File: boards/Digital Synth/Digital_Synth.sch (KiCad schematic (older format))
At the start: 32 parts, among them J5 Barrel_Jack, J6 JTAG, J7 Micro_SD_Card, SW1 SW_Push, SW2 SW_Push, U1 LM1117-3.3, U5 STM32F405RGTx, Y1 12MHz

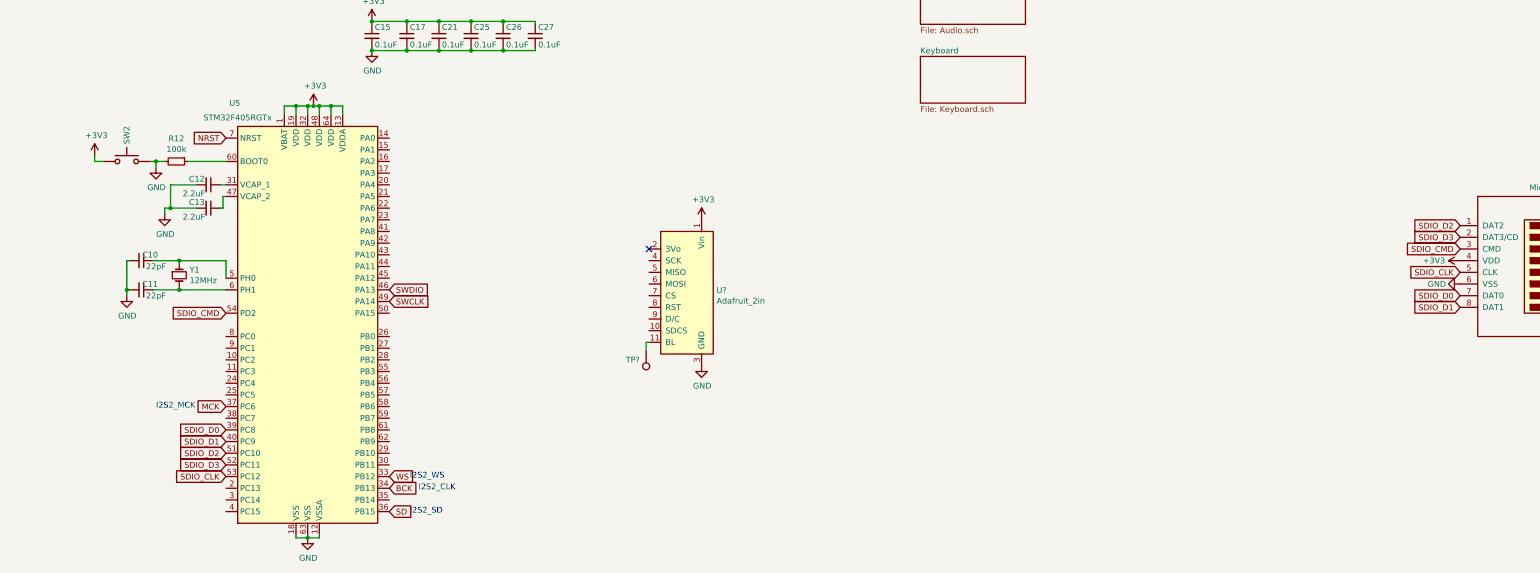
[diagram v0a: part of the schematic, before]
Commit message: added display
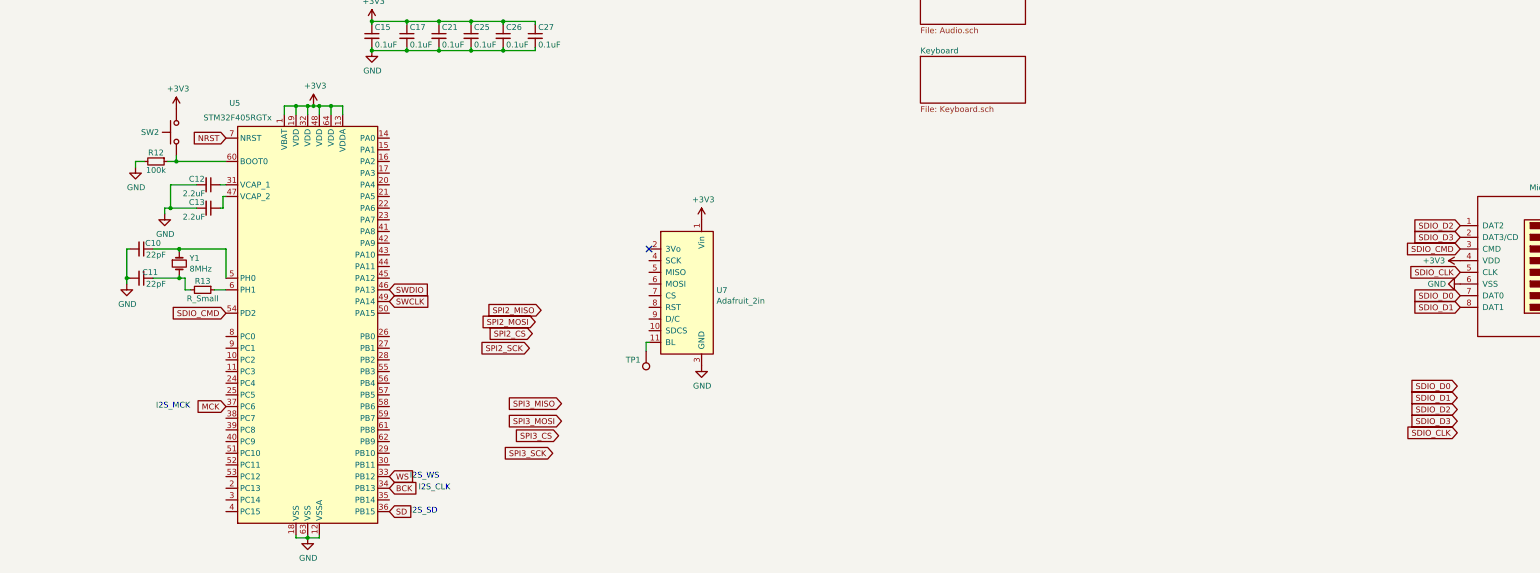
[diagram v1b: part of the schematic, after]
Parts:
- added R13: R_Small, symbol device:R_Small
- C10, C11, C12, C13: footprint (none) -> Capacitor_SMD:C_0603_1608Metric_Pad1.05x0.95mm_HandSolder
- SW1, SW2: footprint (none) -> Button_Switch_THT:SW_PUSH_6mm
- U7: renamed from U?; footprint (none) -> Display:Adafruit_2in
- Y1: value 12MHz -> 8MHz; footprint (none) -> Crystal:Crystal_HC49-U_Vertical
- gave numbers to parts that had none: 1
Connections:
- net +3V3: now also SW2.2; no longer SW2.1
- net GND: no longer SW2.2
- net SDIO_CLK: no longer U5.53 (PC12)
- net SDIO_D0: no longer U5.39 (PC8)
- net SDIO_D1: no longer U5.40 (PC9)
- net SDIO_D2: no longer U5.51 (PC10)
- net SDIO_D3: no longer U5.52 (PC11)
- net at C11.1, Y1.2: now also R13.2; no longer U5.6 (PH1)
- net at R12.1, U5.60 (BOOT0): now also SW2.1
- new net: R13.1, U5.6 (PH1)
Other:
- note added: "I2S_CLK"
- note added: "I2S_MCK"
- note added: "I2S_SD"
- note added: "I2S_WS"
- note removed: "I2S2_CLK"
- note removed: "I2S2_MCK"
- note removed: "I2S2_SD"
- note removed: "I2S2_WS"
- moved on the sheet: C10, C11, R12, SW2, Y1
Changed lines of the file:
@@
-$EndComp
-$Comp
-L MCU_ST_STM32F4:STM32F405RGTx U5
-U 1 1 622C0233
-P 6025 4000
-F 0 "U5" H 5400 5900 50  0000 C CNN
-F 1 "STM32F405RGTx" H 5425 5775 50  0000 C CNN
-F 2 "Package_QFP:LQFP-64_10x10mm_P0.5mm" H 5425 2300 50  0001 R CNN
-F 3 "http://www.st.com/st-web-ui/static/active/en/resource/technical/document/datasheet/DM00037051.pdf" H 6025 4000 50  0001 C CNN
-	1    6025 4000
-	1    0    0    -1
 $EndComp
 $Comp
@@
 L power:GND #PWR016
 U 1 1 622DC5D8
-P 4725 2650
-F 0 "#PWR016" H 4725 2400 50  0001 C CNN
-F 1 "GND" H 4730 2477 50  0000 C CNN
-F 2 "" H 4725 2650 50  0001 C CNN
-F 3 "" H 4725 2650 50  0001 C CNN
-	1    4725 2650
-	1    0    0    -1
-$EndComp
-$Comp
-L device:R_Small R12
-U 1 1 622DDA0B
-P 4900 2600
-F 0 "R12" V 4704 2600 50  0000 C CNN
-F 1 "100k" V 4795 2600 50  0000 C CNN
-F 2 "Resistor_SMD:R_0805_2012Metric_Pad1.15x1.40mm_HandSolder" H 4900 2600 50  0001 C CNN
-F 3 "~" H 4900 2600 50  0001 C CNN
-	1    4900 2600
-	0    1    1    0
-$EndComp
-Wire Wire Line
-	5000 2600 5325 2600
-Wire Wire Line
-	4800 2600 4725 2600
-Wire Wire Line
-	4725 2600 4725 2650
+P 4550 2650
+F 0 "#PWR016" H 4550 2400 50  0001 C CNN
+F 1 "GND" H 4555 2477 50  0000 C CNN
+F 2 "" H 4550 2650 50  0001 C CNN
+F 3 "" H 4550 2650 50  0001 C CNN
+	1    4550 2650
+	1    0    0    -1
+$EndComp
 Text Notes 6900 5625 0    50   ~ 0
-I2S2_SD
+I2S_SD
 Text Notes 6975 5425 0    50   ~ 0
-I2S2_CLK
+I2S_CLK
 Text Notes 6900 5325 0    50   ~ 0
-I2S2_WS
+I2S_WS
 Text Notes 4725 4725 0    50   ~ 0
-I2S2_MCK
+I2S_MCK
 Text GLabel 5325 4700 0    50   Input ~ 0
 MCK
@@
 L device:Crystal_Small Y1
 U 1 1 6252B917
-P 4925 3575
-F 0 "Y1" V 4879 3663 50  0000 L CNN
-F 1 "12MHz" V 4970 3663 50  0000 L CNN
-F 2 "" H 4925 3575 50  0001 C CNN
-F 3 "~" H 4925 3575 50  0001 C CNN
-	1    4925 3575
+P 4925 3475
+F 0 "Y1" V 4879 3563 50  0000 L CNN
+F 1 "8MHz" V 4970 3563 50  0000 L CNN
+F 2 "Crystal:Crystal_HC49-U_Vertical" H 4925 3475 50  0001 C CNN
+F 3 "~" H 4925 3475 50  0001 C CNN
+	1    4925 3475
 	0    1    1    0
 $EndComp
-Wire Wire Line
-	5325 3450 5325 3600
 $Comp
 L device:C_Small C10
 U 1 1 62533AA6
-P 4600 3450
-F 0 "C10" V 4550 3525 50  0000 C CNN
-F 1 "22pF" V 4650 3575 50  0000 C CNN
-F 2 "" H 4600 3450 50  0001 C CNN
-F 3 "~" H 4600 3450 50  0001 C CNN
-	1    4600 3450
+P 4600 3350
+F 0 "C10" V 4550 3450 50  0000 C CNN
+F 1 "22pF" V 4650 3475 50  0000 C CNN
+F 2 "Capacitor_SMD:C_0603_1608Metric_Pad1.05x0.95mm_HandSolder" H 4600 3350 50  0001 C CNN
+F 3 "~" H 4600 3350 50  0001 C CNN
+	1    4600 3350
 	0    1    1    0
 $EndComp
@@
 L device:C_Small C11
 U 1 1 6253A48D
-P 4600 3700
-F 0 "C11" V 4550 3775 50  0000 C CNN
-F 1 "22pF" V 4650 3825 50  0000 C CNN
-F 2 "" H 4600 3700 50  0001 C CNN
-F 3 "~" H 4600 3700 50  0001 C CNN
-	1    4600 3700
+P 4600 3600
+F 0 "C11" V 4550 3675 50  0000 C CNN
+F 1 "22pF" V 4650 3725 50  0000 C CNN
+F 2 "Capacitor_SMD:C_0603_1608Metric_Pad1.05x0.95mm_HandSolder" H 4600 3600 50  0001 C CNN
+F 3 "~" H 4600 3600 50  0001 C CNN
+	1    4600 3600
 	0    1    1    0
 $EndComp
@@
 L power:GND #PWR015
 U 1 1 62542EEB
-P 4475 3750
-F 0 "#PWR015" H 4475 3500 50  0001 C CNN
-F 1 "GND" H 4480 3577 50  0000 C CNN
-F 2 "" H 4475 3750 50  0001 C CNN
-F 3 "" H 4475 3750 50  0001 C CNN
-	1    4475 3750
-	1    0    0    -1
-$EndComp
-Wire Wire Line
-	4500 3700 4475 3700
-Wire Wire Line
-	4475 3700 4475 3750
-Wire Wire Line
-	4500 3450 4475 3450
-Wire Wire Line
-	4475 3450 4475 3700
-Connection ~ 4475 3700
+P 4475 3650
+F 0 "#PWR015" H 4475 3400 50  0001 C CNN
+F 1 "GND" H 4480 3477 50  0000 C CNN
+F 2 "" H 4475 3650 50  0001 C CNN
+F 3 "" H 4475 3650 50  0001 C CNN
+	1    4475 3650
+	1    0    0    -1
+$EndComp
+Wire Wire Line
+	4500 3600 4475 3600
+Wire Wire Line
+	4475 3600 4475 3650
+Wire Wire Line
+	4500 3350 4475 3350
+Wire Wire Line
+	4475 3350 4475 3600
+Connection ~ 4475 3600
 $Comp
 L device:LED_Small D33
@@
 F 0 "SW1" V 1425 4123 50  0000 L CNN
 F 1 "SW_Push" V 1470 4123 50  0001 L CNN
-F 2 "" H 1425 4175 50  0001 C CNN
+F 2 "Button_Switch_THT:SW_PUSH_6mm" H 1425 4175 50  0001 C CNN
 F 3 "" H 1425 4175 50  0001 C CNN
 	1    1425 3975
@@
 L Switch:SW_Push SW2
 U 1 1 62582EF8
-P 4475 2600
-F 0 "SW2" V 4475 2748 50  0000 L CNN
-F 1 "SW_Push" V 4520 2748 50  0001 L CNN
-F 2 "" H 4475 2800 50  0001 C CNN
-F 3 "" H 4475 2800 50  0001 C CNN
-	1    4475 2600
-	1    0    0    -1
-$EndComp
-Wire Wire Line
-	4675 2600 4725 2600
-Connection ~ 4725 2600
+P 4900 2350
+F 0 "SW2" V 4900 2498 50  0000 L CNN
+F 1 "SW_Push" V 4945 2498 50  0001 L CNN
+F 2 "Button_Switch_THT:SW_PUSH_6mm" H 4900 2550 50  0001 C CNN
+F 3 "" H 4900 2550 50  0001 C CNN
+	1    4900 2350
+	0    -1   -1   0
+$EndComp
 $Comp
 L power:+3V3 #PWR014
 U 1 1 6258A598
-P 4200 2550
-F 0 "#PWR014" H 4200 2400 50  0001 C CNN
-F 1 "+3V3" H 4215 2723 50  0000 C CNN
-F 2 "" H 4200 2550 50  0001 C CNN
-F 3 "" H 4200 2550 50  0001 C CNN
-	1    4200 2550
-	1    0    0    -1
-$EndComp
-Wire Wire Line
-	4200 2550 4200 2600
-Wire Wire Line
-	4200 2600 4275 2600
+P 4900 2150
+F 0 "#PWR014" H 4900 2000 50  0001 C CNN
+F 1 "+3V3" H 4915 2323 50  0000 C CNN
+F 2 "" H 4900 2150 50  0001 C CNN
+F 3 "" H 4900 2150 50  0001 C CNN
+	1    4900 2150
+	1    0    0    -1
+$EndComp
 $Comp
 L device:C_Small C12
@@
 F 0 "C12" V 5125 2700 50  0000 C CNN
 F 1 "2.2uF" V 5250 2675 50  0000 C CNN
-F 2 "" H 5175 2800 50  0001 C CNN
+F 2 "Capacitor_SMD:C_0603_1608Metric_Pad1.05x0.95mm_HandSolder" H 5175 2800 50  0001 C CNN
 F 3 "~" H 5175 2800 50  0001 C CNN
 	1    5175 2800
@@
 F 0 "C13" V 5125 2900 50  0000 C CNN
 F 1 "2.2uF" V 5250 2875 50  0000 C CNN
-F 2 "" H 5175 3000 50  0001 C CNN
+F 2 "Capacitor_SMD:C_0603_1608Metric_Pad1.05x0.95mm_HandSolder" H 5175 3000 50  0001 C CNN
 F 3 "~" H 5175 3000 50  0001 C CNN
 	1    5175 3000
@@
 Connection ~ 1550 5550
 Wire Wire Line
-	4700 3700 4925 3700
-Wire Wire Line
-	4700 3450 4925 3450
-Wire Wire Line
-	4925 3475 4925 3450
-Connection ~ 4925 3450
-Wire Wire Line
-	4925 3450 5325 3450
-Wire Wire Line
-	4925 3675 4925 3700
-Connection ~ 4925 3700
-Wire Wire Line
-	4925 3700 5325 3700
+	4700 3600 4925 3600
+Wire Wire Line
+	4700 3350 4925 3350
+Wire Wire Line
+	4925 3375 4925 3350
+Connection ~ 4925 3350
+Wire Wire Line
+	4925 3350 5325 3350
+Wire Wire Line
+	4925 3575 4925 3600
 $Comp
 L Connector:Micro_SD_Card J7
@@
 Text GLabel 15900 3550 0    50   Input ~ 0
 SDIO_CLK
-Text GLabel 5325 4900 0    50   Input ~ 0
+Text GLabel 15875 4525 0    50   Input ~ 0
 SDIO_D0
-Text GLabel 5325 5000 0    50   Input ~ 0
+Text GLabel 15875 4625 0    50   Input ~ 0
 SDIO_D1
-Text GLabel 5325 5100 0    50   Input ~ 0
+Text GLabel 15875 4725 0    50   Input ~ 0
 SDIO_D2
-Text GLabel 5325 5200 0    50   Input ~ 0
+Text GLabel 15875 4825 0    50   Input ~ 0
 SDIO_D3
 Text GLabel 5325 3900 0    50   Input ~ 0
 SDIO_CMD
-Text GLabel 5325 5300 0    50   Input ~ 0
+Text GLabel 15875 4925 0    50   Input ~ 0
 SDIO_CLK
 $Comp
@@
 NoConn ~ 8950 3350
 $Comp
-L power:GND #PWR?
+L power:GND #PWR0110
 U 1 1 623F4583
 P 9400 4350
-F 0 "#PWR?" H 9400 4100 50  0001 C CNN
+F 0 "#PWR0110" H 9400 4100 50  0001 C CNN
 F 1 "GND" H 9405 4177 50  0000 C CNN
 F 2 "" H 9400 4350 50  0001 C CNN
@@
 $EndComp
 $Comp
-L power:+3V3 #PWR?
+L power:+3V3 #PWR0111
 U 1 1 623ECA3D
 P 9400 3100
-F 0 "#PWR?" H 9400 2950 50  0001 C CNN
+F 0 "#PWR0111" H 9400 2950 50  0001 C CNN
 F 1 "+3V3" H 9415 3273 50  0000 C CNN
 F 2 "" H 9400 3100 50  0001 C CNN
@@
 $EndComp
 $Comp
-L Connector:TestPoint TP?
+L Connector:TestPoint TP1
 U 1 1 6240D6CD
 P 8925 4225
-F 0 "TP?" H 9100 4300 50  0000 R CNN
+F 0 "TP1" H 9100 4300 50  0000 R CNN
 F 1 "TestPoint" H 8867 4342 50  0001 R CNN
 F 2 "" H 9125 4225 50  0001 C CNN
@@
 $EndComp
 $Comp
-L Display_Graphic:Adafruit_2in U?
+L Display_Graphic:Adafruit_2in U7
 U 1 1 623EB93B
 P 9050 3150
-F 0 "U?" H 9528 2596 50  0000 L CNN
+F 0 "U7" H 9528 2596 50  0000 L CNN
 F 1 "Adafruit_2in" H 9528 2505 50  0000 L CNN
-F 2 "" H 8900 3150 50  0001 C CNN
+F 2 "Display:Adafruit_2in" H 8900 3150 50  0001 C CNN
 F 3 "" H 8900 3150 50  0001 C CNN
 	1    9050 3150
@@
 Wire Wire Line
 	8925 4150 8925 4225
+$Comp
+L device:R_Small R12
+U 1 1 622DDA0B
+P 4725 2600
+F 0 "R12" V 4650 2600 50  0000 C CNN
+F 1 "100k" V 4800 2600 50  0000 C CNN
+F 2 "Resistor_SMD:R_0805_2012Metric_Pad1.15x1.40mm_HandSolder" H 4725 2600 50  0001 C CNN
+F 3 "~" H 4725 2600 50  0001 C CNN
+	1    4725 2600
+	0    1    1    0
+$EndComp
+Wire Wire Line
+	4625 2600 4550 2600
+Wire Wire Line
+	4550 2600 4550 2650
+Wire Wire Line
+	4825 2600 4900 2600
+Wire Wire Line
+	4900 2600 4900 2550
+Wire Wire Line
+	4900 2600 5325 2600
+Connection ~ 4900 2600
+Text GLabel 8025 3875 0    50   Input ~ 0
+SPI2_MISO
+Text GLabel 7975 3975 0    50   Input ~ 0
+SPI2_MOSI
+Text GLabel 7950 4075 0    50   Input ~ 0
+SPI2_CS
+Text GLabel 7925 4200 0    50   Input ~ 0
+SPI2_SCK
+Text GLabel 8200 4675 0    50   Input ~ 0
+SPI3_MISO
+Text GLabel 8200 4825 0    50   Input ~ 0
+SPI3_MOSI
+Text GLabel 8175 4950 0    50   Input ~ 0
+SPI3_CS
+Text GLabel 8125 5100 0    50   Input ~ 0
+SPI3_SCK
+$Comp
+L device:R_Small R13
+U 1 1 624AF75A
+P 5125 3700
+F 0 "R13" V 5050 3700 50  0000 C CNN
+F 1 "R_Small" V 5200 3700 50  0000 C CNN
+F 2 "" H 5125 3700 50  0001 C CNN
+F 3 "~" H 5125 3700 50  0001 C CNN
+	1    5125 3700
+	0    1    1    0
+$EndComp
+$Comp
+L MCU_ST_STM32F4:STM32F405RGTx U5
+U 1 1 622C0233
+P 6025 4000
+F 0 "U5" H 5400 5900 50  0000 C CNN
+F 1 "STM32F405RGTx" H 5425 5775 50  0000 C CNN
+F 2 "Package_QFP:LQFP-64_10x10mm_P0.5mm" H 5425 2300 50  0001 R CNN
+F 3 "http://www.st.com/st-web-ui/static/active/en/resource/technical/document/datasheet/DM00037051.pdf" H 6025 4000 50  0001 C CNN
+	1    6025 4000
+	1    0    0    -1
+$EndComp
+Wire Wire Line
+	5325 3350 5325 3600
+Wire Wire Line
+	4925 3600 4975 3600
+Wire Wire Line
+	4975 3600 4975 3700
+Wire Wire Line
+	4975 3700 5025 3700
+Connection ~ 4925 3600
+Wire Wire Line
+	5225 3700 5325 3700
 $EndSCHEMATC

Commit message: almost done with layout
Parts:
- removed C2, C9: 1uF, symbol device:C_Small
- removed J7: Micro_SD_Card, symbol Connector:Micro_SD_Card
- removed SW2: SW_Push, Button_Switch_THT:SW_PUSH_6mm, symbol Switch:SW_Push
- removed U7: Adafruit_2in, Display:Adafruit_2in, symbol Display_Graphic:Adafruit_2in
- added C2, C9: 10uF, Capacitor_THT:CP_Radial_D5.0mm_P2.00mm, symbol device:CP_Small
- added J7: UART_Debug, Connector_PinHeader_2.54mm:PinHeader_1x02_P2.54mm_Vertical, symbol Connector:Conn_01x02_Male
- added J9: UART_MIDI, Connector_PinHeader_2.54mm:PinHeader_1x02_P2.54mm_Vertical, symbol Connector:Conn_01x02_Male
- added U8: Adafruit_2.4in, Display:Adafruit_2.4in, symbol Display_Graphic:Adafruit_2.4in
- D31, D32, D33: footprint (none) -> Diode_SMD:D_0805_2012Metric_Pad1.15x1.40mm_HandSolder
- J5: value Barrel_Jack -> 5V IN; footprint (none) -> Connector_BarrelJack:BarrelJack_CUI_PJ-102AH_Horizontal
- R10, R11, R9: value R_Small -> 470; footprint (none) -> Resistor_SMD:R_0603_1608Metric_Pad1.05x0.95mm_HandSolder
- R12, R8: footprint Resistor_SMD:R_0805_2012Metric_Pad1.15x1.40mm_HandSolder -> Resistor_SMD:R_0603_1608Metric_Pad1.05x0.95mm_HandSolder
- R13: footprint (none) -> Resistor_SMD:R_0603_1608Metric_Pad1.05x0.95mm_HandSolder
- TP1: footprint (none) -> TestPoint:TestPoint_Pad_1.0x1.0mm
- U1: footprint (none) -> Package_TO_SOT_SMD:SOT-223
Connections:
- net +3V3: now also C9.1
- net +5V: now also C2.1, U8.2 (Vin)
- net BCK: now also U5.51 (PC10); no longer U5.34 (PB13)
- net GND: now also C2.2, C9.2, U8.1 (GND)
- net MCK: now also U5.38 (PC7); no longer U5.37 (PC6)
- net SD: now also U5.53 (PC12); no longer U5.36 (PB15)
- net SPI2_CS: now also U5.33 (PB12)
- net SPI2_MISO: now also U5.35 (PB14)
- net SPI2_MOSI: now also U5.36 (PB15)
- net SPI2_SCK: now also U5.34 (PB13)
- net WS: now also U5.50 (PA15); no longer U5.33 (PB12)
- net B8: now reaches U5.10 (PC2)
- net B9: now reaches U5.11 (PC3)
- net RV1: now reaches U5.14 (PA0)
- net RV2: now reaches U5.15 (PA1)
- net RV3: now reaches U5.16 (PA2)
- net RV4: now reaches U5.17 (PA3)
- net B3: now reaches U5.2 (PC13)
- net RV5: now reaches U5.20 (PA4)
- net RV6: now reaches U5.21 (PA5)
- net RV7: now reaches U5.22 (PA6)
- net RV8: now reaches U5.23 (PA7)
- net Y+: now reaches U5.24 (PC4)
- net Y+: now also U8.11 (Y+)
- net X+: now reaches U5.25 (PC5)
- net X+: now also U8.12 (X+)
- net Y-: now reaches U5.26 (PB0)
- net Y-: now also U8.13 (Y-)
- net X-: now reaches U5.27 (PB1)
- net X-: now also U8.14 (X-)
- net TX_Debug: now reaches U5.29 (PB10)
- net TX_Debug: now also J7.1 (Pin_1)
- net B4: now reaches U5.3 (PC14)
- net RX_Debug: now reaches U5.30 (PB11)
- net RX_Debug: now also J7.2 (Pin_2)
- net B5: now reaches U5.4 (PC15)
- net TX_MIDI: now reaches U5.42 (PA9)
- net TX_MIDI: now also J9.1 (Pin_1)
- net RX_MIDI: now reaches U5.43 (PA10)
- net RX_MIDI: now also J9.2 (Pin_2)
- net at U5.44 (PA11): now also R9.1
- net at U5.45 (PA12): now also R10.1
- net SPI1_SCK: now reaches U5.55 (PB3)
- net SPI1_SCK: now also U8.4 (CLK)
- net SPI1_MISO: now reaches U5.56 (PB4)
- net SPI1_MISO: now also U8.5 (MISO)
- net SPI1_MOSI: now reaches U5.57 (PB5)
- net SPI1_MOSI: now also U8.6 (MOSI)
- net SPI1_CS2: now reaches U5.58 (PB6)
- net SPI1_CS2: now also U8.7 (CS)
- net SPI1_CS1: now reaches U5.59 (PB7)
- net SPI1_CS1: now also U8.19 (CCS)
- net at R12.1, U5.60 (BOOT0): now also TP1.1
- net B1: now reaches U5.61 (PB8)
- net B2: now reaches U5.62 (PB9)
- net B6: now reaches U5.8 (PC0)
- net B7: now reaches U5.9 (PC1)
- net SDIO_CMD renamed DC
- net DC: now also U8.8 (D/C)
- no-connect marks 1 -> 30
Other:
- note added: "Analog"
- note added: "I2S_CK"
- note removed: "I2S_CLK"
- moved on the sheet: C10, C11, C12, C13, C15, C17, C21, C25, C26, C27, C3, C6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

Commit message: finished layout
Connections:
- net RV1: now also U5.17 (PA3); no longer U5.14 (PA0)
- net RV2: now also U5.16 (PA2); no longer U5.15 (PA1)
- net RV3: now also U5.15 (PA1); no longer U5.16 (PA2)
- net RV4: now also U5.14 (PA0); no longer U5.17 (PA3)
- net WS renamed LRCLK
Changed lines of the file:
@@
 Text Notes 4875 5175 2    50   ~ 0
 I2S_CK
-Text Notes 6700 3975 0    50   ~ 0
+Text Notes 6825 4000 0    50   ~ 0
 I2S_WS
 Text Notes 4525 4875 0    50   ~ 0
@@
 Text GLabel 5125 5150 0    50   Input ~ 0
 BCK
-Text GLabel 6525 3950 2    50   Input ~ 0
-WS
 $Comp
 L power:+5V #PWR07
@@
 Text GLabel 5125 4450 0    50   Input ~ 0
 B9
+Text GLabel 6525 2750 2    50   Input ~ 0
+RV1
+Text GLabel 6525 2650 2    50   Input ~ 0
+RV2
+Text GLabel 6525 2550 2    50   Input ~ 0
+RV3
 Text GLabel 6525 2450 2    50   Input ~ 0
-RV1
-Text GLabel 6525 2550 2    50   Input ~ 0
-RV2
-Text GLabel 6525 2650 2    50   Input ~ 0
-RV3
-Text GLabel 6525 2750 2    50   Input ~ 0
 RV4
 Text GLabel 6525 2850 2    50   Input ~ 0
@@
 Wire Wire Line
 	4725 2650 5125 2650
+Text GLabel 6525 3950 2    50   Input ~ 0
+LRCLK
 $EndSCHEMATC
